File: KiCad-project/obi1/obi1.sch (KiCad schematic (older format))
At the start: 9 parts, among them J1 USB, U1 RG3V3, U2 REG1V2

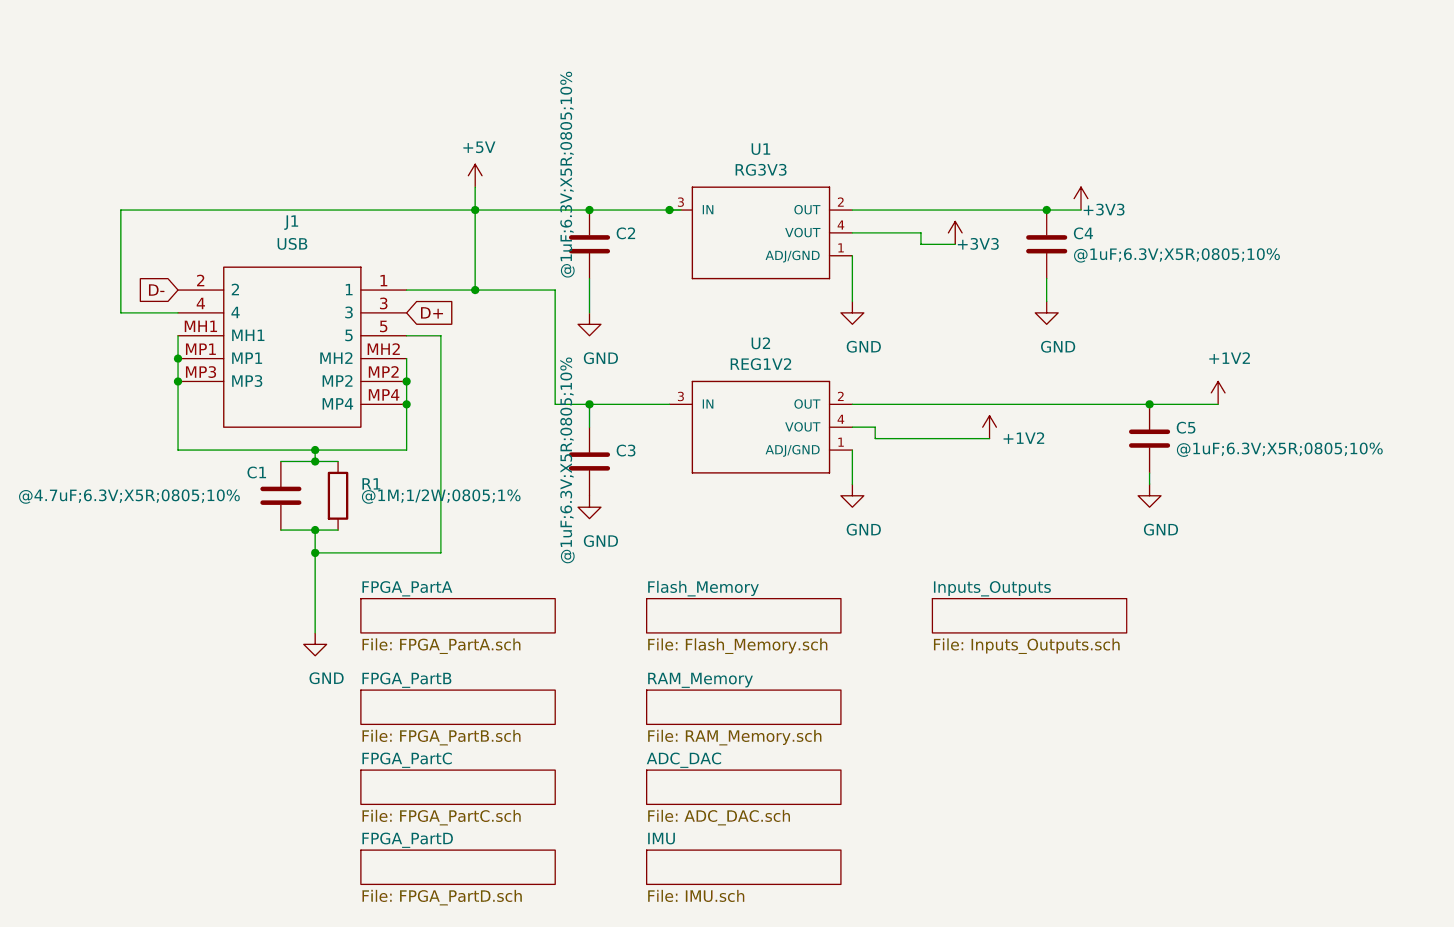
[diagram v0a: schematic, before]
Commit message: Text in  Silk layer adjusted
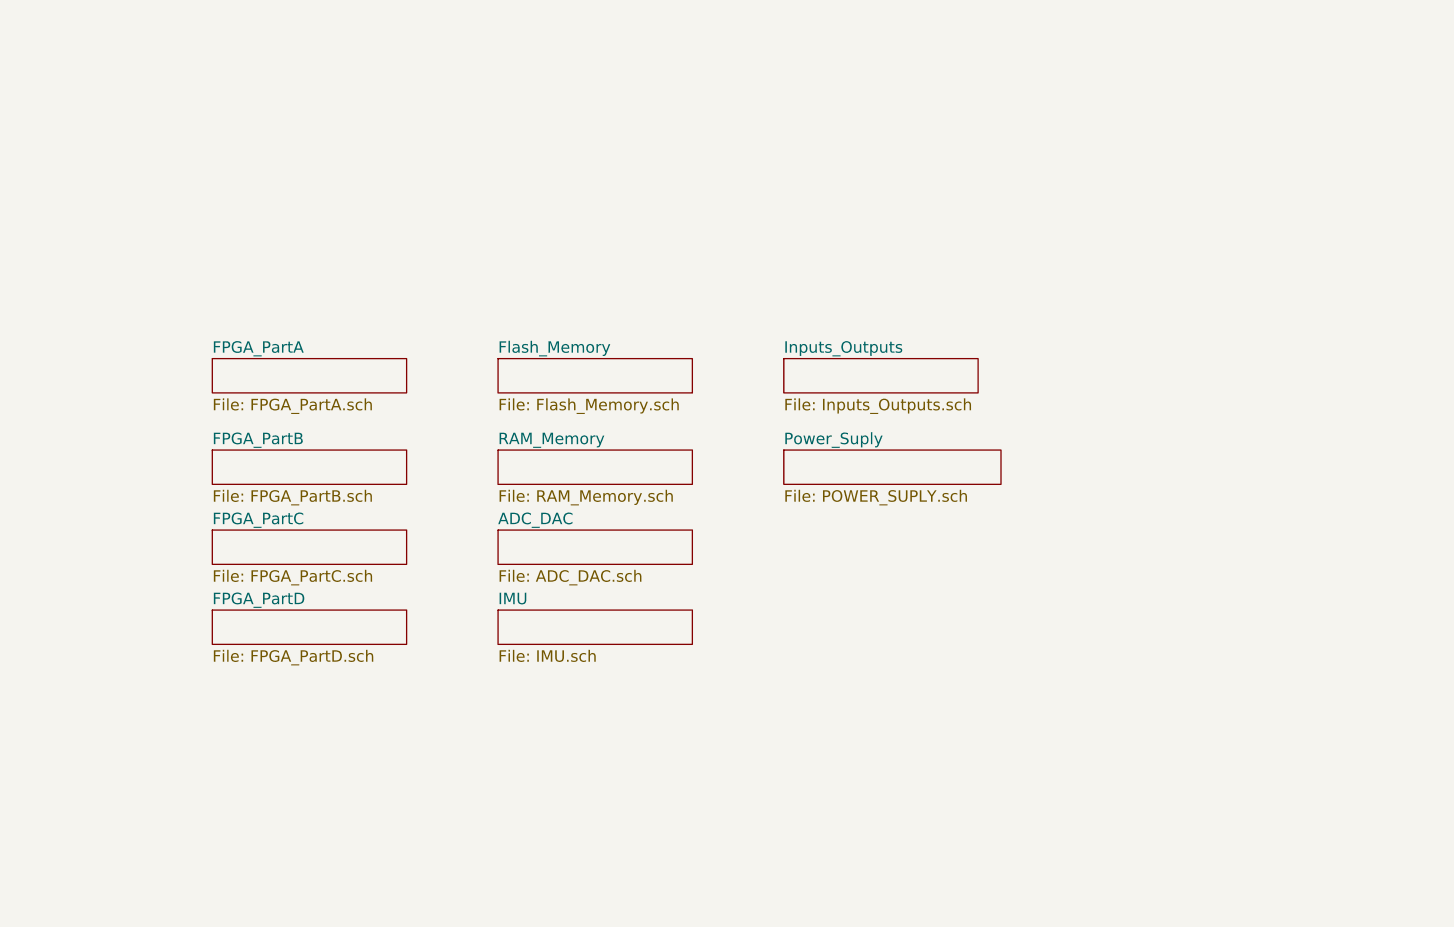
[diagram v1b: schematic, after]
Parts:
- removed C1: @4.7uF;6.3V;X5R;0805;10%, Capacitor_SMD:C_0805_2012Metric_Pad1.18x1.45mm_HandSolder, symbol Device:C
- removed C2, C3, C4, C5: @1uF;6.3V;X5R;0805;10%, Capacitor_SMD:C_0805_2012Metric_Pad1.18x1.45mm_HandSolder, symbol Device:C
- removed J1: USB, egalan_lib:101181930001LF, symbol egalan:10118193-0001LF
- removed R1: @1M;1/2W;0805;1%, Resistor_SMD:R_0805_2012Metric_Pad1.20x1.40mm_HandSolder, symbol Device:R
- removed U1: RG3V3, egalan_lib:SOT230P700X180-4N3.3, symbol obi1-rescue:AZ1117EH-3.3TRG1-egalan
- removed U2: REG1V2, egalan_lib:SOT230P700X180-4N1.2, symbol obi1-rescue:AZ1117EH-1.2TRG1-egalan
